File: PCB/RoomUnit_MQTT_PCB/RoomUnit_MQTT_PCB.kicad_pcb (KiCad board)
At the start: 2 copper layers, 34.3 x 60 mm, 25 parts, among them J1 Conn_01x07_Socket, J2 Conn_01x07_Socket, Q1 MMBTA06, U1 LMV393, U3 L78L24_SOT89

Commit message: applied schematic changes (wip)
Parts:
- removed D1: BAS40-04, Package_TO_SOT_SMD:SOT-23
- removed D2: D, Diode_SMD:D_0805_2012Metric
- removed U3: L78L24_SOT89, Package_TO_SOT_SMD:SOT-89-3
- added R15: 33k, Resistor_SMD:R_0805_2012Metric_Pad1.20x1.40mm_HandSolder, F.Cu at (169.8, 46.7)
- added R16: 1k, Resistor_SMD:R_0805_2012Metric_Pad1.20x1.40mm_HandSolder, F.Cu at (169.8, 50.7)
- added R4: 4.7k, Resistor_SMD:R_0805_2012Metric_Pad1.20x1.40mm_HandSolder, F.Cu at (169.3, 63.4)
- added R7: 1M, Resistor_SMD:R_0805_2012Metric_Pad1.20x1.40mm_HandSolder, F.Cu at (165.7, 44.1)
- added U2: TLV61046ADB, Package_TO_SOT_SMD:SOT-23-6, F.Cu at (165.7, 47.2)
- L1: value L -> 10u; footprint Inductor_SMD:L_Ferrocore_DLG-0705 -> Inductor_SMD:L_APV_APH0420
- R2: value 690k -> 680k
- R6: value 9.2k -> 8.2k
- moved C2 14.8 mm to (172.9, 64.4), turned to -90 degrees
- moved R9 11.7 mm to (165.7, 64.4), turned to 90 degrees
- moved L1 11.3 mm to (165.7, 51.7), turned to 0 degrees
- moved C3 8.82 mm to (161.7, 50.7), turned to -90 degrees
- moved C4 3.59 mm to (161.7, 46.7), turned to 90 degrees
- moved C1 0.20 mm to (169.3, 66.0)
- moved U1 0.20 mm to (169.3, 70.0)
- moved Q1 0.10 mm to (176.4, 64.4), turned to 90 degrees
- moved R6 0.10 mm to (176.4, 72.1)
- moved R5 0.09 mm to (176.4, 70.0)
- moved R8 0.08 mm to (176.4, 68.0)
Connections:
- L1 pad 1: Net-(D2-K) -> +5V
- L1 pad 2: Net-(Q1-C) -> Net-(U2-SW)
- Q1 pad 3: Net-(Q1-C) -> MPS
- U4 pad 5: unconnected-(U4-VCC_OUT-Pad5) -> AO1
- U4 pad 6: AO1 -> AO2
- U4 pad 7: AO2 -> AO3
- U4 pad 8: AO3 -> unconnected-(U4-Pad8)
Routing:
- net MPS: track 16.6 -> 30.7 mm
- net Net-(D2-K): track 9.06 -> 0.00 mm
- net +5V: track 70.9 -> 62.8 mm
- net Net-(U2-FB): track 0.00 -> 6.46 mm
- net +24V: track 11.7 -> 16.8 mm
- net AO1: track 57.2 -> 62.3 mm
- net +3V3: track 58.3 -> 63.2 mm
- net Net-(Q1-C): track 4.56 -> 0.00 mm
- net Net-(Q1-B): track 7.53 -> 3.59 mm
- net Net-(U2-SW): track 0.00 -> 3.92 mm
- net AO2: track 50.4 -> 53.9 mm
- net AO3: track 44.2 -> 46.3 mm
- net Net-(R15-Pad2): track 0.00 -> 2.06 mm
- net GND: track 0.00 -> 1.40 mm, vias 18 -> 49
- net Net-(J1-Pin_7): track 3.61 -> 2.60 mm
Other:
- outline, holes or cut-outs redrawn

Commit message: PCB improvements
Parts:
- C3: value 330n -> 1u; footprint Capacitor_SMD:C_0805_2012Metric_Pad1.18x1.45mm_HandSolder -> Capacitor_SMD:C_1206_3216Metric
- C4: value 100n -> 4.7u; footprint Capacitor_SMD:C_0805_2012Metric_Pad1.18x1.45mm_HandSolder -> Capacitor_SMD:C_1206_3216Metric
- moved R1 4.99 mm to (162.5, 69.0), turned to 0 degrees
- moved R14 3.11 mm to (162.5, 75.1)
- moved R3 3.08 mm to (162.5, 73.1)
- moved R2 3.04 mm to (162.5, 71.0)
- moved R8 2.03 mm to (176.4, 70.0)
- moved R4 2.03 mm to (169.3, 65.5)
- moved C1 2.03 mm to (169.3, 68.0)
- moved C2 2.03 mm to (172.9, 66.5)
- moved Q1 2.03 mm to (176.4, 66.5)
- moved R5 2.03 mm to (176.4, 72.1)
- moved R6 2.03 mm to (176.4, 74.1)
- moved R9 2.03 mm to (165.7, 66.5)
- moved U1 2.03 mm to (169.3, 72.1)
- moved C3 0.56 mm to (161.5, 51.2)
- moved C4 0.45 mm to (161.5, 46.2)
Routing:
- net +3V3: track 63.2 -> 55.4 mm
- net Net-(J2-Pin_7): track 20.3 -> 14.6 mm
- net UART_TX: track 21.7 -> 19.7 mm
- net UART_RX: track 13.1 -> 11.6 mm
- net MPS: track 30.7 -> 31.6 mm
- net Net-(U1A--): track 11.6 -> 11.0 mm
- net GND: vias 49 -> 58

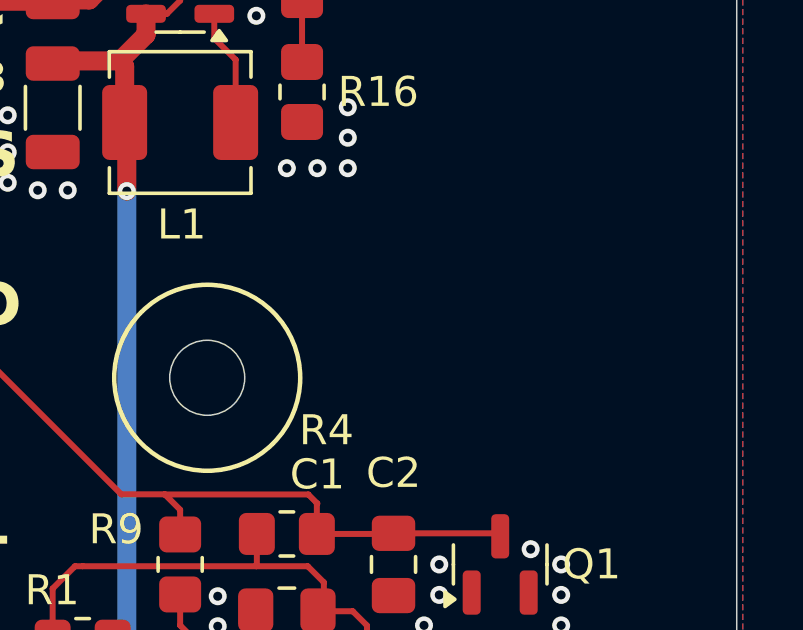
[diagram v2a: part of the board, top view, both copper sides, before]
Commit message: schematic updated 18V
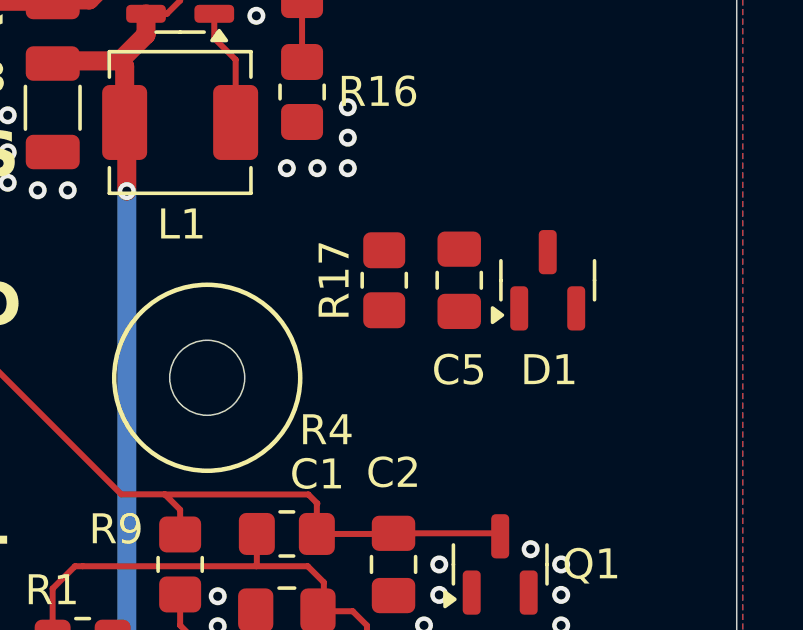
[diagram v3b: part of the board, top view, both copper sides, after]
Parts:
- added C5: 100n, Capacitor_SMD:C_0805_2012Metric_Pad1.18x1.45mm_HandSolder, F.Cu at (175.1, 57.0)
- added D1: BZX84C18, Package_TO_SOT_SMD:SOT-23, F.Cu at (178.0, 57.0)
- added R17: 1.2k, Resistor_SMD:R_0805_2012Metric_Pad1.20x1.40mm_HandSolder, F.Cu at (172.6, 57.0)
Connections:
- R4 pad 1: +3V3 -> +18V

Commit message: SChematic update - PCB almost done
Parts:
- R16: value 1k -> 1.6k
- moved R17 16.5 mm to (166.2, 41.8), turned to 0 degrees
- moved C5 15.3 mm to (169.5, 42.8)
- moved D1 15.2 mm to (172.8, 42.8)
- moved C2 3.74 mm to (169.2, 65.5), turned to 180 degrees
- moved R4 3.60 mm to (172.8, 66.5), turned to -90 degrees
- moved R5 1.90 mm to (177.5, 70.5), turned to -90 degrees
- moved R8 1.49 mm to (175.0, 70.5), turned to -90 degrees
- moved C3 0.50 mm to (162.0, 51.2)
- moved C4 0.50 mm to (162.0, 46.2)
- moved L1 0.50 mm to (166.2, 51.7)
- moved R16 0.50 mm to (170.3, 50.7)
- moved R7 0.50 mm to (166.2, 44.1)
- moved U2 0.50 mm to (166.2, 47.2)
- moved R15 0.45 mm to (170.2, 46.8)
- moved R6 0.19 mm to (176.2, 74.0)
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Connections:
- R2 pad 2: Net-(U1A--) -> Net-(U1A-+)
- R3 pad 2: Net-(U1A-+) -> Net-(U1A--)
- R6 pad 1: Net-(U1A-+) -> Net-(U1A--)
- R9 pad 1: Net-(U1A--) -> Net-(U1A-+)
- U1 pad 5: Net-(U1A-+) -> Net-(U1A--)
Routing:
- net +18V: track 0.00 -> 29.2 mm
- net Net-(Q1-B): track 3.59 -> 11.4 mm
- net +3V3: track 55.4 -> 52.5 mm
- net +24V: track 16.8 -> 19.6 mm
- net GND: track 1.40 -> 3.92 mm, vias 58 -> 114
- net Net-(U2-FB): track 6.46 -> 5.21 mm
- net MPS: track 31.6 -> 32.5 mm

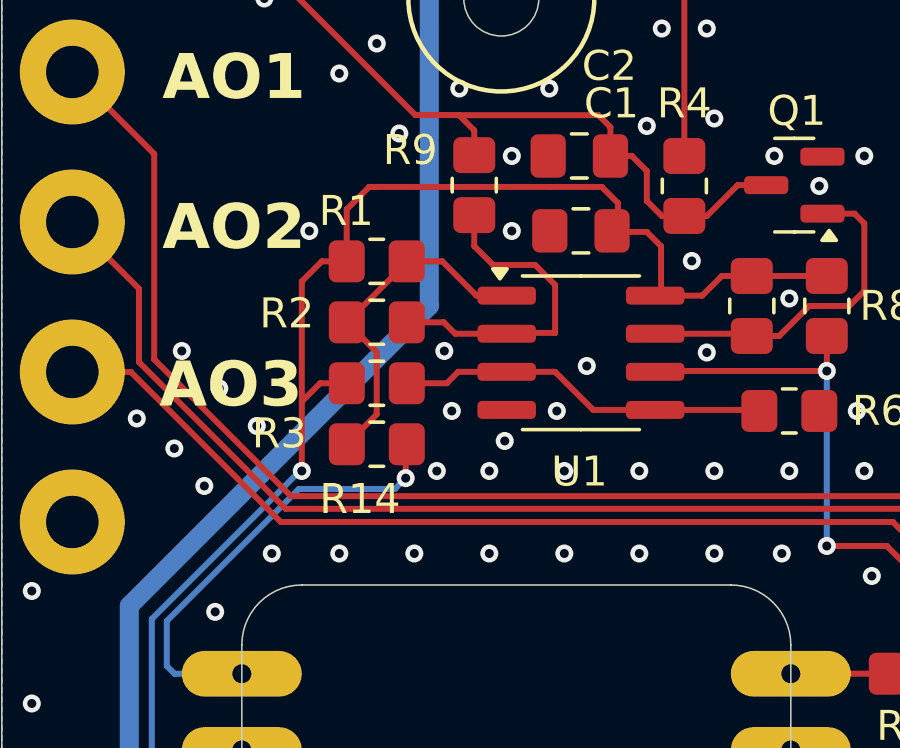
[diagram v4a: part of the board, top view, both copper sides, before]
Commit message: added all jlc components
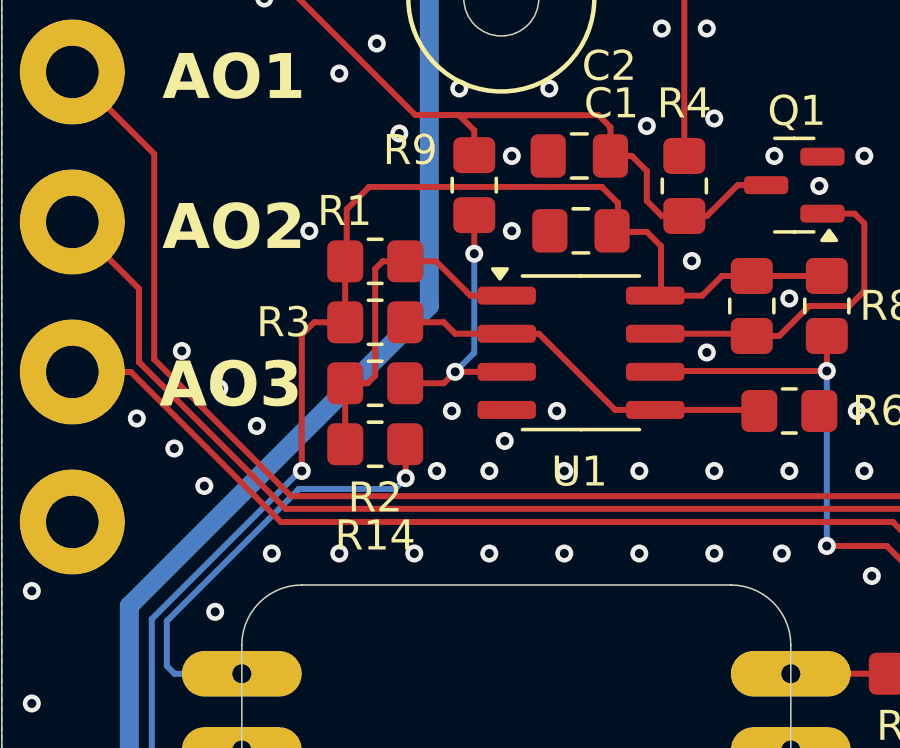
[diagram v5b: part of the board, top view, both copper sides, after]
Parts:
- moved R2 2.03 mm to (162.4, 73.1)
- moved R3 2.03 mm to (162.4, 71.0)
- moved R14 0.05 mm to (162.4, 75.1)
- moved R1 0.05 mm to (162.4, 69.0)
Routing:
- net Net-(U1A-+): track 12.5 -> 9.03 mm, vias 0 -> 2
- net Net-(U1A--): track 11.0 -> 13.1 mm
- net +3V3: track 52.5 -> 50.9 mm
- net GND: vias 114 -> 112

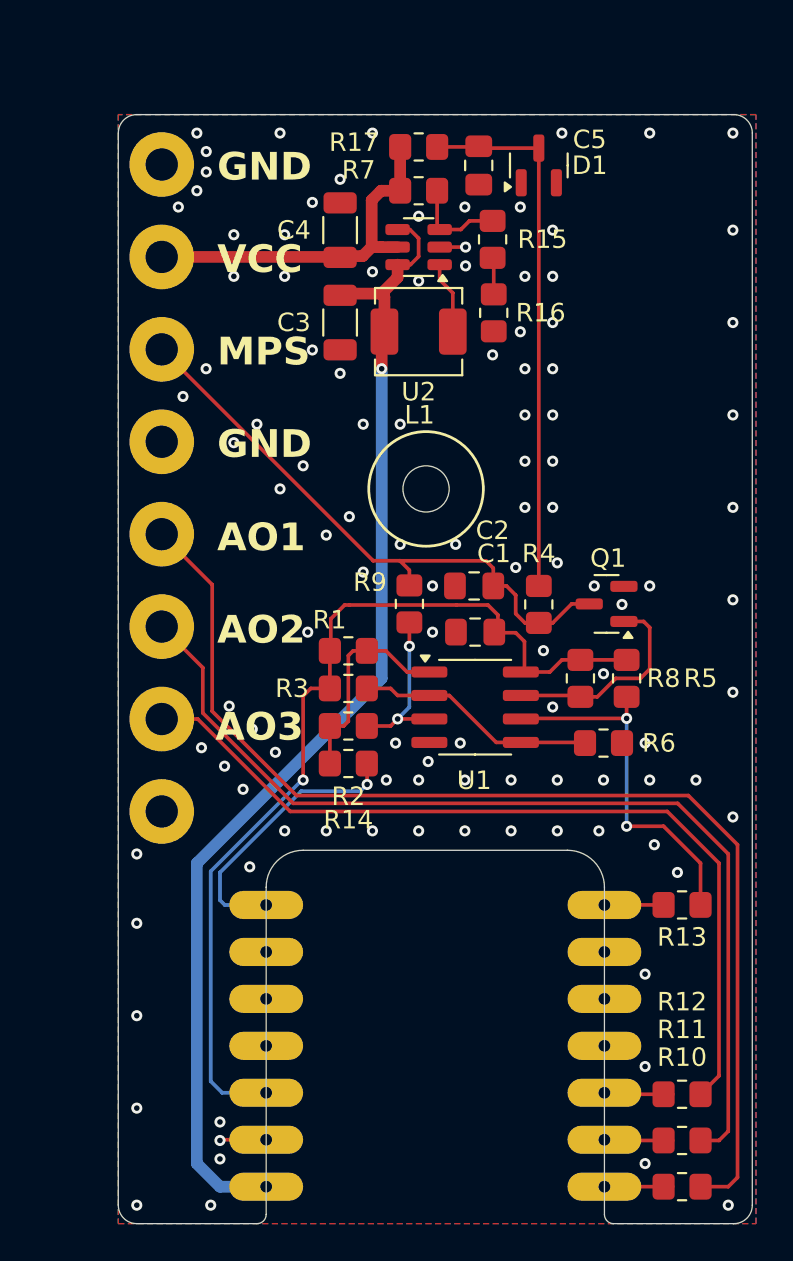
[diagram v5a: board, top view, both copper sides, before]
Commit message: Spannungsteiler AOx
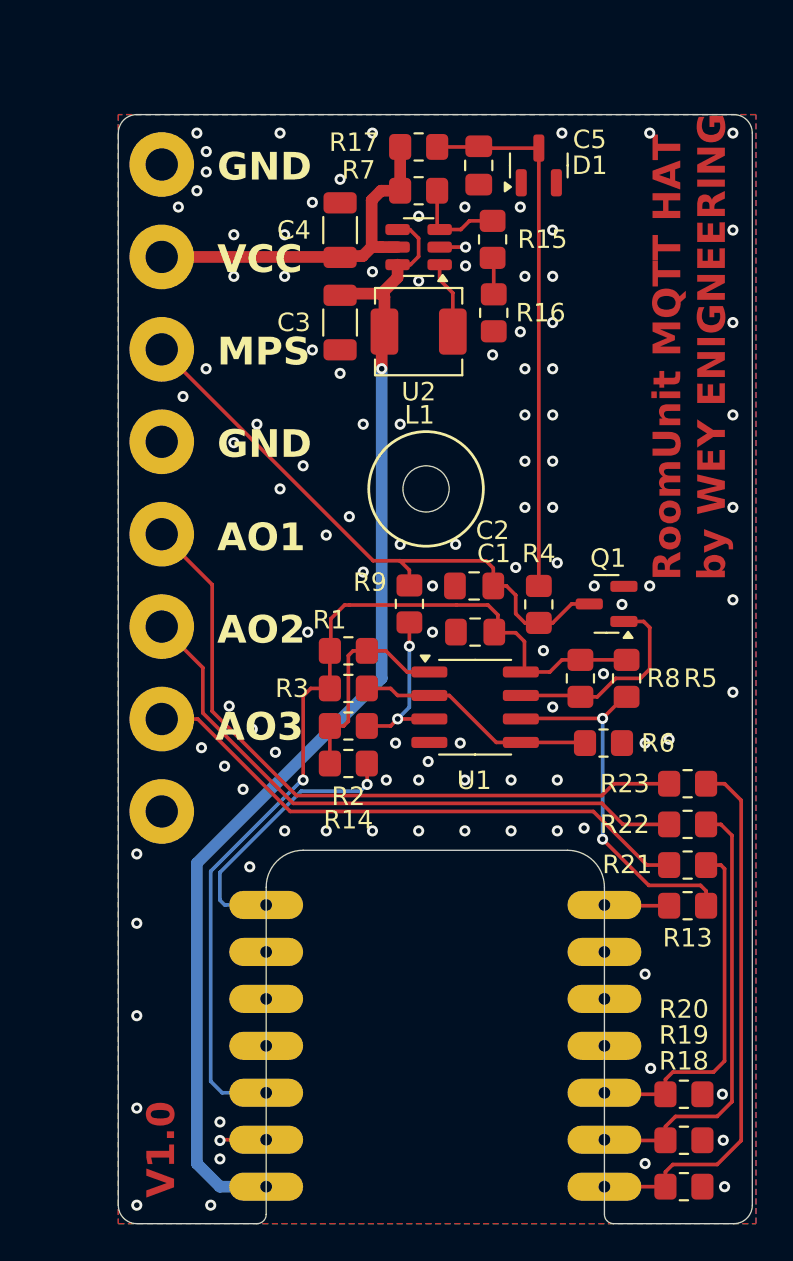
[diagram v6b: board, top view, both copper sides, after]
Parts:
- removed R10, R11, R12: 0, Resistor_SMD:R_0805_2012Metric_Pad1.20x1.40mm_HandSolder
- added R18: 10k, Resistor_SMD:R_0805_2012Metric_Pad1.20x1.40mm_HandSolder, F.Cu at (180.6, 98.0)
- added R19: 10k, Resistor_SMD:R_0805_2012Metric_Pad1.20x1.40mm_HandSolder, F.Cu at (180.6, 95.5)
- added R20: 10k, Resistor_SMD:R_0805_2012Metric_Pad1.20x1.40mm_HandSolder, F.Cu at (180.6, 93.0)
- added R21: 10k, Resistor_SMD:R_0805_2012Metric_Pad1.20x1.40mm_HandSolder, F.Cu at (180.8, 80.6)
- added R22: 10k, Resistor_SMD:R_0805_2012Metric_Pad1.20x1.40mm_HandSolder, F.Cu at (180.8, 78.4)
- added R23: 10k, Resistor_SMD:R_0805_2012Metric_Pad1.20x1.40mm_HandSolder, F.Cu at (180.8, 76.2)
- moved R13 0.30 mm to (180.8, 82.8)
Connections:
- J1 pad 1: Net-(J1-Pin_1) -> AO1
- J1 pad 2: Net-(J1-Pin_2) -> AO2
- J1 pad 3: Net-(J1-Pin_3) -> AO3
- U4 pad 5: AO1 -> Net-(U4-AO1)
- U4 pad 6: AO2 -> Net-(U4-AO2)
- U4 pad 7: AO3 -> Net-(U4-AO3)
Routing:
- net Net-(U4-AO1): track 0.00 -> 37.4 mm
- net Net-(U4-AO2): track 0.00 -> 33.1 mm
- net AO1: track 62.3 -> 29.6 mm
- net Net-(U4-AO3): track 0.00 -> 30.5 mm
- net AO2: track 53.9 -> 24.3 mm
- net AO3: track 46.3 -> 19.2 mm
- net Net-(J1-Pin_3): track 3.13 -> 0.00 mm
- net Net-(J1-Pin_2): track 3.12 -> 0.00 mm
- net Net-(J1-Pin_1): track 3.10 -> 0.00 mm
- net Net-(J1-Pin_7): track 2.60 -> 3.52 mm
- net GND: vias 112 -> 109
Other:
- board text added: "RoomUnit MQTT HAT by WEY ENIGNEERING"
- board text added: "V1.0"

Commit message: 3D assembly
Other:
- board text added: "Room Unit MQTT HAT by WEY ENIGNEERING"
- board text removed: "RoomUnit MQTT HAT by WEY ENIGNEERING"
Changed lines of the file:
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@@
 		(layer "Edge.Cuts")
 	)
-	(gr_text "RoomUnit MQTT HAT\nby WEY ENIGNEERING"
+	(gr_text "Room Unit MQTT HAT\nby WEY ENIGNEERING"
 		(at 183 65.2 90)
 		(layer "F.Cu")
@@
 		)
 	)
-	(gr_text "RoomUnit MQTT HAT\nby WEY ENIGNEERING"
+	(gr_text "Room Unit MQTT HAT\nby WEY ENIGNEERING"
 		(at 183 65.2 90)
 		(layer "F.Mask")

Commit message: DRC passed
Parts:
- moved R19 0.20 mm to (180.4, 95.5)
- moved R18 0.20 mm to (180.4, 98.0)
- moved R20 0.20 mm to (180.4, 93.0)
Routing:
- net AO1: track 29.6 -> 29.0 mm
- net AO3: track 19.2 -> 18.6 mm
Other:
- board text added: "Room Unit MQTT HAT by WEY ENGINEERING"
- board text removed: "Room Unit MQTT HAT by WEY ENIGNEERING"
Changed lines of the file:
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@@
 	(footprint "Resistor_SMD:R_0805_2012Metric_Pad1.20x1.40mm_HandSolder"
 		(layer "F.Cu")
-		(at 180.600991 95.489489)
+		(at 180.4 95.489489)
 		(descr "Resistor SMD 0805 (2012 Metric), square (rectangular) end terminal, IPC_7351 nominal with elongated pad for handsoldering. (Body size source: IPC-SM-782 page 72, https://www.pcb-3d.com/wordpress/wp-content/uploads/ipc-sm-782a_amendment_1_and_2.pdf), generated with kicad-footprint-generator")
 		(tags "resistor handsolder")
@@
 	(footprint "Resistor_SMD:R_0805_2012Metric_Pad1.20x1.40mm_HandSolder"
 		(layer "F.Cu")
-		(at 180.6 98)
+		(at 180.4 98)
 		(descr "Resistor SMD 0805 (2012 Metric), square (rectangular) end terminal, IPC_7351 nominal with elongated pad for handsoldering. (Body size source: IPC-SM-782 page 72, https://www.pcb-3d.com/wordpress/wp-content/uploads/ipc-sm-782a_amendment_1_and_2.pdf), generated with kicad-footprint-generator")
 		(tags "resistor handsolder")
@@
 	(footprint "Resistor_SMD:R_0805_2012Metric_Pad1.20x1.40mm_HandSolder"
 		(layer "F.Cu")
-		(at 180.6 93)
+		(at 180.4 93)
 		(descr "Resistor SMD 0805 (2012 Metric), square (rectangular) end terminal, IPC_7351 nominal with elongated pad for handsoldering. (Body size source: IPC-SM-782 page 72, https://www.pcb-3d.com/wordpress/wp-content/uploads/ipc-sm-782a_amendment_1_and_2.pdf), generated with kicad-footprint-generator")
 		(tags "resistor handsolder")
@@
 		(layer "Edge.Cuts")
 	)
-	(gr_text "Room Unit MQTT HAT\nby WEY ENIGNEERING"
-		(at 183 65.2 90)
+	(gr_text "Room Unit MQTT HAT\nby WEY ENGINEERING"
+		(at 182.8 65.2 90)
 		(layer "F.Cu")
 		(effects
@@
 		)
 	)
-	(gr_text "Room Unit MQTT HAT\nby WEY ENIGNEERING"
-		(at 183 65.2 90)
+	(gr_text "Room Unit MQTT HAT\nby WEY ENGINEERING"
+		(at 182.8 65.2 90)
 		(layer "F.Mask")
 		(effects
@@
 	)
 	(via
-		(at 182.8 98)
+		(at 182.4 98)
 		(size 0.6)
 		(drill 0.3)
@@
 	)
 	(via
-		(at 151 93.75)
+		(at 151 93.2)
 		(size 0.6)
 		(drill 0.3)
@@
 	)
 	(via
-		(at 182.727827 95.487756)
+		(at 182.4 95.487756)
 		(size 0.6)
 		(drill 0.3)
@@
 	)
 	(via
-		(at 182.68249 92.993421)
+		(at 182.4 93)
 		(size 0.6)
 		(drill 0.3)
@@
 	)
 	(via
-		(at 178.75 41)
+		(at 177.8 41)
 		(size 0.6)
 		(drill 0.3)
@@
 	)
 	(segment
-		(start 180 93)
+		(start 179.4 93)
 		(end 176.98 93)
 		(width 0.2)
@@
 	)
 	(segment
+		(start 176.98 93)
+		(end 176.9 92.92)
+		(width 0.2)
+		(layer "F.Cu")
+		(net 8)
+	)
+	(segment
 		(start 182.2 91.8)
 		(end 182.8 91.2)
@@
 	)
 	(segment
-		(start 176.98 93)
-		(end 176.9 92.92)
-		(width 0.2)
-		(layer "F.Cu")
-		(net 8)
-	)
-	(segment
 		(start 182.8 76.2)
 		(end 181.6 76.2)
@@
 	)
 	(segment
+		(start 179.4 98)
+		(end 176.9 98)
+		(width 0.2)
+		(layer "F.Cu")
+		(net 9)
+	)
+	(segment
 		(start 183.699 77.099)
 		(end 182.8 76.2)
@@
 	)
 	(segment
-		(start 180 98)
-		(end 176.9 98)
+		(start 180 96.8)
+		(end 182.4 96.8)
 		(width 0.2)
 		(layer "F.Cu")
@@
 	)
 	(segment
-		(start 180 96.8)
-		(end 182.4 96.8)
+		(start 182.6 78.4)
+		(end 181.6 78.4)
 		(width 0.2)
 		(layer "F.Cu")
-		(net 9)
+		(net 10)
 	)
 	(segment
-		(start 176.94 95.5)
-		(end 176.9 95.46)
+		(start 179.4 94.6)
+		(end 179.8 94.2)
 		(width 0.2)
 		(layer "F.Cu")
@@
 	)
 	(segment
-		(start 179.600991 95.489489)
-		(end 179.600991 94.744249)
+		(start 183.2 93.4)
+		(end 183.2 79)
 		(width 0.2)
 		(layer "F.Cu")
@@
 	)
 	(segment
-		(start 179.600991 94.744249)
-		(end 180.14524 94.2)
+		(start 183.2 79)
+		(end 182.6 78.4)
 		(width 0.2)
 		(layer "F.Cu")
@@
 	)
 	(segment
-		(start 183.2 93.4)
-		(end 183.2 79)
+		(start 179.4 95.489489)
+		(end 179.389489 95.5)
 		(width 0.2)
 		(layer "F.Cu")
@@
 	)
 	(segment
-		(start 180.14524 94.2)
+		(start 179.8 94.2)
 		(end 182.4 94.2)
 		(width 0.2)
@@
 	)
 	(segment
-		(start 182.4 94.2)
-		(end 183.2 93.4)
+		(start 179.4 95.489489)
+		(end 179.4 94.6)
 		(width 0.2)
 		(layer "F.Cu")
@@
 	)
 	(segment
-		(start 182.6 78.4)
-		(end 181.6 78.4)
+		(start 176.94 95.5)
+		(end 176.9 95.46)
 		(width 0.2)
 		(layer "F.Cu")
@@
 	)
 	(segment
-		(start 180 95.5)
+		(start 179.389489 95.5)
 		(end 176.94 95.5)
 		(width 0.2)
@@
 	)
 	(segment
-		(start 183.2 79)
-		(end 182.6 78.4)
+		(start 182.4 94.2)
+		(end 183.2 93.4)
 		(width 0.2)
 		(layer "F.Cu")
